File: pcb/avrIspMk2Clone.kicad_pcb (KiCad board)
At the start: 2 copper layers, 50 x 40 mm, 44 parts, among them IC1 ATMEGA8-16AU, J1 DB9, P1 USB_OTG, P2 CONN_01X03, P3 CONN_01X02, P4 CONN_02X05, P5 CONN_02X03, SW1 SW_SPDT, U1 LM1117-3.3, Y1 12MHz

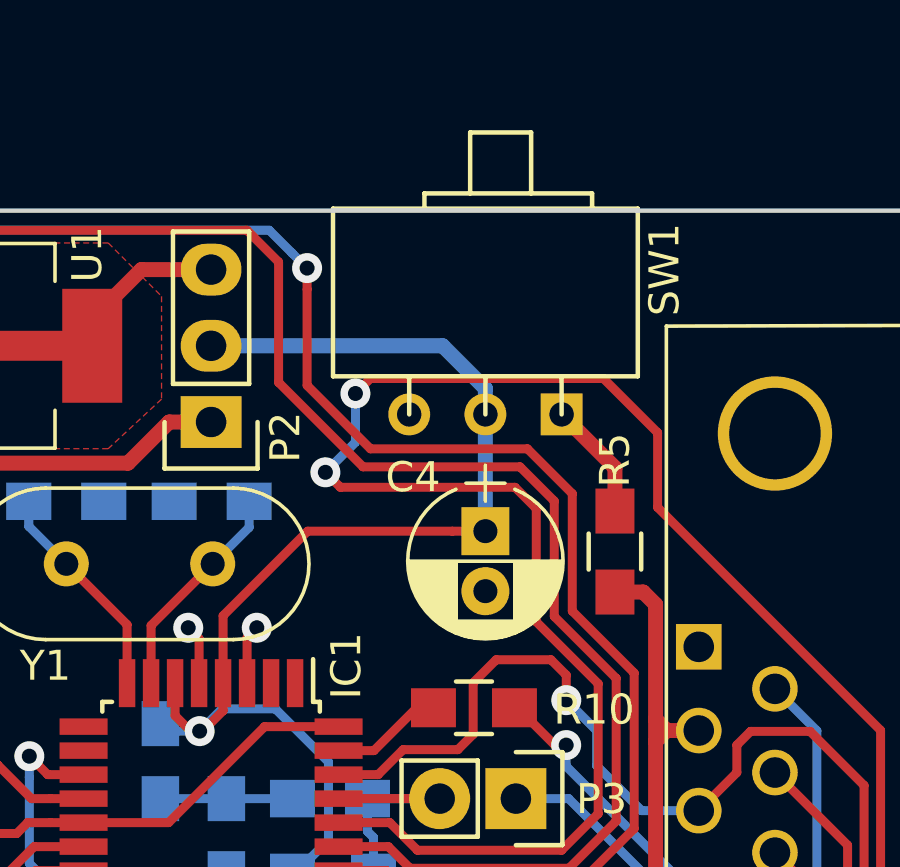
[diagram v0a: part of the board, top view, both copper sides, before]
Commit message: Changed the Slide Switch to a Model from Pollin
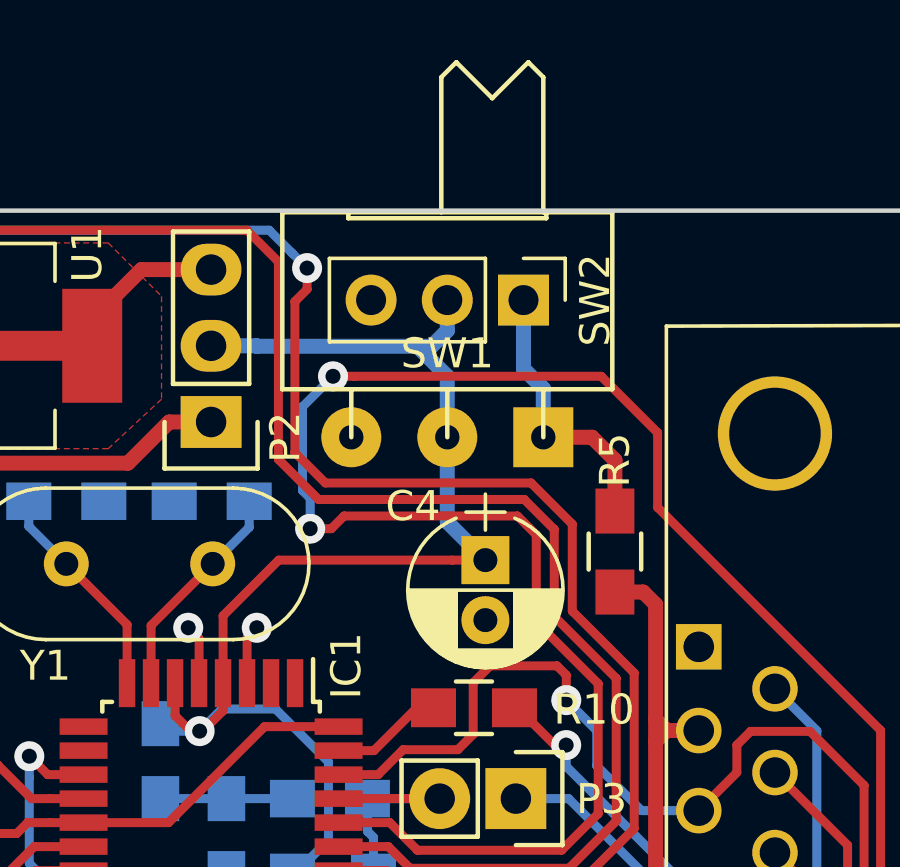
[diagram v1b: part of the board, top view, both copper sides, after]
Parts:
- removed G***: LOGO, proz_logo:Shimatta_SolderMask
- removed REF***: KiCad-Logo_6mm_SilkScreen, Symbols:KiCad-Logo_6mm_SilkScreen
- removed REF***: ESD-Logo_6.6x6mm_SilkScreen, Symbols:ESD-Logo_6.6x6mm_SilkScreen
- added SW2: SW_SPDT, Pin_Headers:Pin_Header_Straight_1x03_Pitch2.54mm, F.Cu at (113.7, 88.0)
- SW1: footprint Buttons_Switches_THT:SW_Micro_SPST_Angled -> proz_switch:SW_Micro_Slide_3.8
- moved SW1 1.48 mm to (111.2, 92.6)
- moved C4 0.97 mm to (112.4, 96.7)
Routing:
- net Net-(R5-Pad1): track 3.96 -> 9.25 mm
- net /LED_BLUE: track 123.0 -> 125.7 mm
- net VCC: track 48.0 -> 50.3 mm
- net /LED_GREEN: track 69.8 -> 71.1 mm
- net /LED_RED: track 71.6 -> 72.6 mm

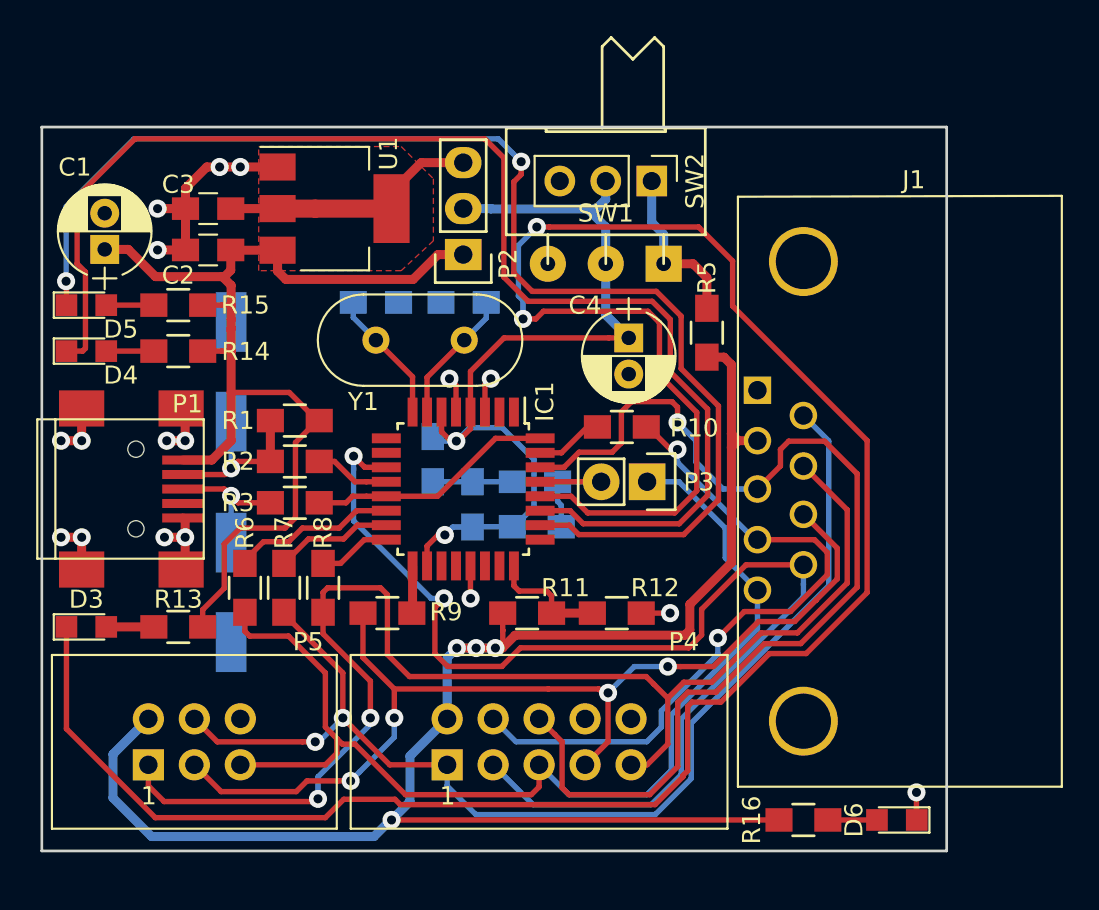
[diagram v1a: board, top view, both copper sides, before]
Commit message: changed resistors and caps from 0805 to 0603
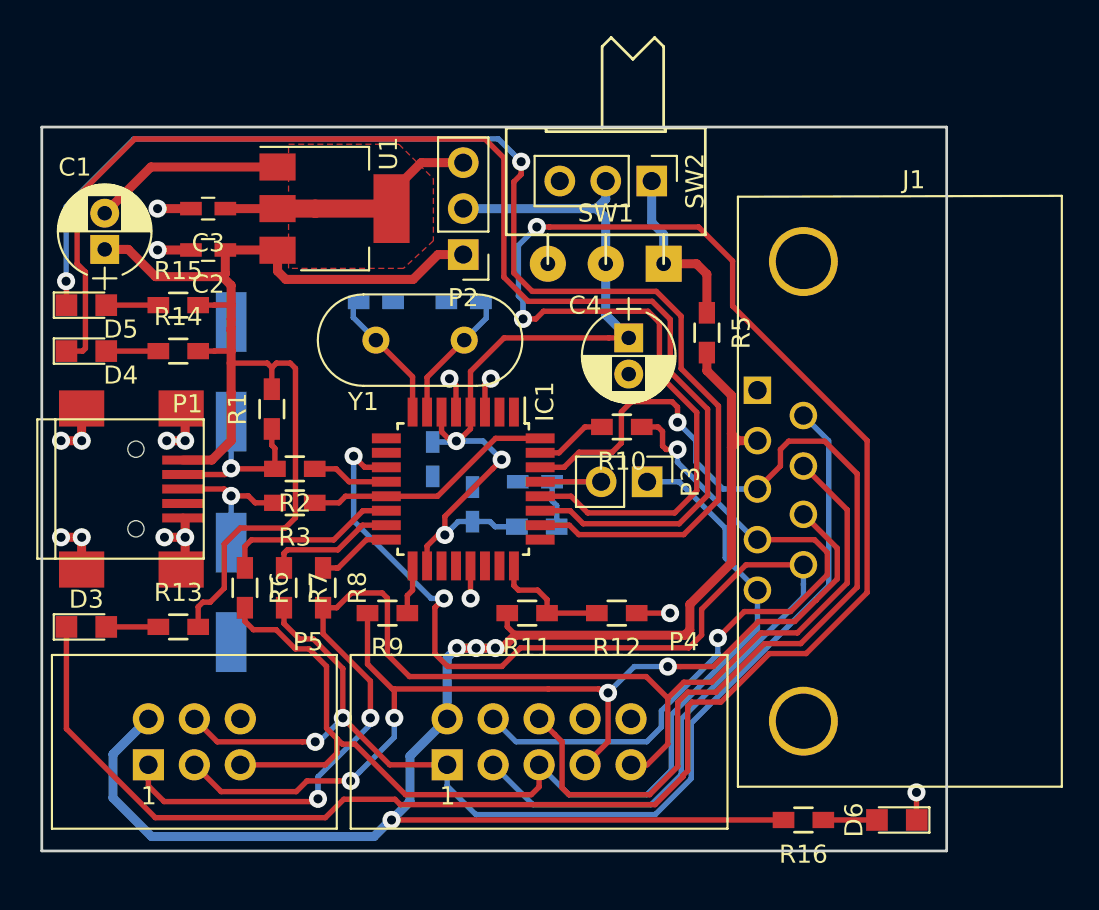
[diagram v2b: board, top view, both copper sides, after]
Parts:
- C2, C3, C5, C6, C7, C8, C9: footprint Capacitors_SMD:C_0805_HandSoldering -> Capacitors_SMD:C_0603_HandSoldering
- P2: footprint Socket_Strips:Socket_Strip_Straight_1x03 -> Pin_Headers:Pin_Header_Straight_1x03_Pitch2.54mm
- P3: footprint Socket_Strips:Socket_Strip_Straight_1x02 -> Pin_Headers:Pin_Header_Straight_1x02_Pitch2.54mm
- R1, R10, R11, R12, R13, R14, R15, R16, R2, R3, R4, R6, R7, R8, R9: footprint Resistors_SMD:R_0805_HandSoldering -> Resistors_SMD:R_0603_HandSoldering
- R5: value 10 -> 1; footprint Resistors_SMD:R_0805_HandSoldering -> Resistors_SMD:R_0603_HandSoldering
- moved R1 1.42 mm to (92.7, 100.6), turned to 90 degrees
- moved R2 0.41 mm to (94.0, 103.9)
- turned P2 to 180 degrees
- turned P3 to 270 degrees
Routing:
- net +5V: track 60.4 -> 63.2 mm
- net GND: track 38.3 -> 36.3 mm, vias 17 -> 15
- net VCC: track 50.3 -> 49.5 mm, vias 2 -> 3
- net /MISO_OUT: track 73.3 -> 72.6 mm
- net /TXD_OUT: track 38.4 -> 39.1 mm
- net Net-(IC1-Pad14): track 9.12 -> 9.82 mm
- net /MOSI_OUT: track 63.2 -> 63.9 mm
- net Net-(IC1-Pad15): track 6.53 -> 7.11 mm
- net /VCC_OUT: track 90.8 -> 90.3 mm
